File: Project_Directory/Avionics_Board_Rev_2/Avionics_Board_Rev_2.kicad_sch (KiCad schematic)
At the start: 0 parts

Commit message: started working.
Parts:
- added U1: Teensy4.1, symbol VelR:Teensy4.1_1
- added U2: ~, symbol VelR:RFM95W
- added U3: ~, symbol VelR:ADXL-377
- added U4: ~, symbol VelR:NEO-7M

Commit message: temp
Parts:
- removed U4: ~, symbol VelR:NEO-7M
- added U5: ~, symbol VelR:BUCK_CONVERTER
- added U6: ~, symbol VelR:neo-7m
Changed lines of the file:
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@@
 	(paper "A4")
-	(symbol
-		(lib_id "VelR:NEO-7M")
-		(at 237.49 110.49 0)
-		(unit 1)
-		(exclude_from_sim no)
-		(in_bom yes)
-		(on_board yes)
-		(dnp no)
-		(fields_autoplaced yes)
-		(property "Reference" "U4"
-			(at 254 105.3398 0)
-			(effects
-				(font
-					(size 1.27 1.27)
-				)
-			)
-		)
-		(property "Value" "~"
-			(at 254 107.8798 0)
-			(effects
-				(font
-					(size 1.27 1.27)
-				)
-			)
-		)
-		(property "Footprint" ""
-			(at 237.49 110.49 0)
-			(effects
-				(font
-					(size 1.27 1.27)
-				)
-				(hide yes)
-			)
-		)
-		(property "Datasheet" ""
-			(at 237.49 110.49 0)
-			(effects
-				(font
-					(size 1.27 1.27)
-				)
-				(hide yes)
-			)
-		)
-		(property "Description" ""
-			(at 237.49 110.49 0)
-			(effects
-				(font
-					(size 1.27 1.27)
-				)
-				(hide yes)
-			)
-		)
-		(pin "4"
-		)
-		(pin "1"
-		)
-		(pin "3"
-		)
-		(pin "2"
-		)
-		(instances
-			(project ""
-				(path "/d97b3dcb-6a87-4cc6-862f-281d47ed4b8f"
-					(reference "U4")
-					(unit 1)
-				)
-			)
-		)
-	)
 	(symbol
 		(lib_id "VelR:Teensy4.1_1")
@@
 					(unit 1)
 				)
+			)
+		)
+	)
+	(symbol
+		(lib_id "VelR:neo-7m")
+		(at 213.36 107.95 0)
+		(unit 1)
+		(exclude_from_sim no)
+		(in_bom yes)
+		(on_board yes)
+		(dnp no)
+		(fields_autoplaced yes)
+		(property "Reference" "U6"
+			(at 213.36 107.95 0)
+			(effects
+				(font
+					(size 1.27 1.27)
+				)
+				(hide yes)
+			)
+		)
+		(property "Value" "~"
+			(at 219.71 107.9499 0)
+			(effects
+				(font
+					(size 1.27 1.27)
+				)
+				(justify left)
+			)
+		)
+		(property "Footprint" ""
+			(at 213.36 107.95 0)
+			(effects
+				(font
+					(size 1.27 1.27)
+				)
+				(hide yes)
+			)
+		)
+		(property "Datasheet" ""
+			(at 213.36 107.95 0)
+			(effects
+				(font
+					(size 1.27 1.27)
+				)
+				(hide yes)
+			)
+		)
+		(property "Description" ""
+			(at 213.36 107.95 0)
+			(effects
+				(font
+					(size 1.27 1.27)
+				)
+				(hide yes)
+			)
+		)
+		(pin "1"
+		)
+		(pin "3"
+		)
+		(pin "4"
+		)
+		(pin "2"
+		)
+		(instances
+			(project ""
+				(path "/d97b3dcb-6a87-4cc6-862f-281d47ed4b8f"
+					(reference "U6")
+					(unit 1)
+				)
+			)
+		)
+	)
+	(symbol
+		(lib_id "VelR:BUCK_CONVERTER")
+		(at 55.88 96.52 0)
+		(unit 1)
+		(exclude_from_sim no)
+		(in_bom yes)
+		(on_board yes)
+		(dnp no)
+		(fields_autoplaced yes)
+		(property "Reference" "U5"
+			(at 56.515 85.09 0)
+			(effects
+				(font
+					(size 1.27 1.27)
+				)
+			)
+		)
+		(property "Value" "~"
+			(at 56.515 87.63 0)
+			(effects
+				(font
+					(size 1.27 1.27)
+				)
+			)
+		)
+		(property "Footprint" ""
+			(at 55.88 96.52 0)
+			(effects
+				(font
+					(size 1.27 1.27)
+				)
+				(hide yes)
+			)
+		)
+		(property "Datasheet" ""
+			(at 55.88 96.52 0)
+			(effects
+				(font
+					(size 1.27 1.27)
+				)
+				(hide yes)
+			)
+		)
+		(property "Description" ""
+			(at 55.88 96.52 0)
+			(effects
+				(font
+					(size 1.27 1.27)
+				)
+				(hide yes)
+			)
+		)
+		(pin "6"
+		)
+		(pin "4"
+		)
+		(pin "1"
+		)
+		(pin "8"
+		)
+		(pin "5"
+		)
+		(pin "3"
+		)
+		(pin "2"
+		)
+		(pin "7"
+		)
+		(instances
+			(project ""
+				(path "/d97b3dcb-6a87-4cc6-862f-281d47ed4b8f"
+					(reference "U5")
+					(unit 1)
+				)

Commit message: schematic
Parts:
- removed U5: ~, symbol VelR:BUCK_CONVERTER
- added Buck_Converter: ~, symbol VelR3:BUCK_CONVERTER_new
- added J1: Battery, symbol Connector:Conn_01x02_Pin
- added J10: PWM_1, symbol Connector:Conn_01x03_Pin
- added J11: PWM_2, symbol Connector:Conn_01x03_Pin
- added J12: PWM_3, symbol Connector:Conn_01x03_Pin
- added J13: I2C, symbol Connector:Conn_01x04_Pin
- added J14: UART, symbol Connector:Conn_01x04_Pin
- added J2: ARM, symbol Connector:Conn_01x02_Pin
- added J3: PYRO_1, symbol Connector:Conn_01x02_Pin
- added J7: PWM_4, symbol Connector:Conn_01x03_Pin
- added J8: PWM_5, symbol Connector:Conn_01x03_Pin
- added J9: PWM_6, symbol Connector:Conn_01x03_Pin
- added Q1: IRF026, symbol Simulation_SPICE:NMOS
- added Q2: Drive_MOS, symbol Simulation_SPICE:NMOS
- added R1, R2, R3, R4, R5: R, symbol Device:R
- added U4: AMS1117-5.0, Package_TO_SOT_SMD:SOT-223-3_TabPin2, symbol Regulator_Linear:AMS1117-5.0
- added U5: AMS1117-3.3, Package_TO_SOT_SMD:SOT-223-3_TabPin2, symbol Regulator_Linear:AMS1117-3.3
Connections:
- net +3.3V: now reaches U1.51 (3V3)
- net +3.3V: now also U2.4 (3.3V), U3.2 (3.3V), U6.1 (VCC), J13.1 (Pin_1), J14.1 (Pin_1), R3.2
- net GND: now reaches U1.52 (GND)
- net GND: now also U2.7 (GND), U6.4 (GND), J10.3 (Pin_3), J11.3 (Pin_3), J12.3 (Pin_3), J13.4 (Pin_4), J14.4 (Pin_4), J7.3 (Pin_3), J8.3 (Pin_3), J9.3 (Pin_3), Q2.3 (S), R5.2
- new net: Q1.2 (G), Q2.1 (D), R1.2
- new net: Buck_Converter.1 (Vin), Buck_Converter.2 (Vin)
- new net: Buck_Converter.3 (Vin), Buck_Converter.4 (Vin)
- new net: J3.1 (Pin_1), Q1.1 (D), R4.1
- new net +5V: J10.2 (Pin_2), J11.2 (Pin_2), J12.2 (Pin_2), J7.2 (Pin_2), J8.2 (Pin_2), J9.2 (Pin_2)
- new net +BATT: Buck_Converter.5 (Vout), Buck_Converter.6 (Vout), J1.1 (Pin_1), J2.1 (Pin_1), R2.1
- new net +VDC: J2.2 (Pin_2), J3.2 (Pin_2), R1.1, R2.2
- new net GNDPWR: Buck_Converter.7 (Vout), Buck_Converter.8 (Vout), J1.2 (Pin_2), Q1.3 (S)
- new net PYRO_1_Trig: Q2.2 (G), R3.1
- new net PYRO_1_continuity: R4.2, R5.1

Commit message: working
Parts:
- added D1: B120-E3, Diode_SMD:D_SMA, symbol VelR7:B120-E3
- added U7: ~, symbol VelR8:gy-91
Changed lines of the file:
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@@
+	)
+	(symbol
+		(lib_id "VelR7:B120-E3")
+		(at 229.87 99.06 0)
+		(unit 1)
+		(exclude_from_sim no)
+		(in_bom yes)
+		(on_board yes)
+		(dnp no)
+		(fields_autoplaced yes)
+		(property "Reference" "D1"
+			(at 229.5525 92.71 0)
+			(effects
+				(font
+					(size 1.27 1.27)
+				)
+			)
+		)
+		(property "Value" "B120-E3"
+			(at 229.5525 95.25 0)
+			(effects
+				(font
+					(size 1.27 1.27)
+				)
+			)
+		)
+		(property "Footprint" "Diode_SMD:D_SMA"
+			(at 229.87 103.505 0)
+			(effects
+				(font
+					(size 1.27 1.27)
+				)
+				(hide yes)
+			)
+		)
+		(property "Datasheet" "http://www.vishay.com/docs/88946/b120.pdf"
+			(at 229.87 99.06 0)
+			(effects
+				(font
+					(size 1.27 1.27)
+				)
+				(hide yes)
+			)
+		)
+		(property "Description" "20V 1A Schottky Barrier Rectifier Diode, SMA(DO-214AC)"
+			(at 229.87 99.06 0)
+			(effects
+				(font
+					(size 1.27 1.27)
+				)
+				(hide yes)
+			)
+		)
+		(pin "1"
+		)
+		(pin "2"
+		)
+		(instances
+			(project ""
+				(path "/d97b3dcb-6a87-4cc6-862f-281d47ed4b8f"
+					(reference "D1")
+					(unit 1)
+				)
+			)
+		)
 	)
 	(symbol
@@
 					(unit 1)
 				)
+			)
+		)
+	)
+	(symbol
+		(lib_id "VelR8:gy-91")
+		(at 193.04 82.55 0)
+		(unit 1)
+		(exclude_from_sim no)
+		(in_bom yes)
+		(on_board yes)
+		(dnp no)
+		(fields_autoplaced yes)
+		(property "Reference" "U7"
+			(at 201.93 81.2799 0)
+			(effects
+				(font
+					(size 1.27 1.27)
+				)
+				(justify left)
+			)
+		)
+		(property "Value" "~"
+			(at 201.93 83.8199 0)
+			(effects
+				(font
+					(size 1.27 1.27)
+				)
+				(justify left)
+			)
+		)
+		(property "Footprint" ""
+			(at 193.04 82.55 0)
+			(effects
+				(font
+					(size 1.27 1.27)
+				)
+				(hide yes)
+			)
+		)
+		(property "Datasheet" ""
+			(at 193.04 82.55 0)
+			(effects
+				(font
+					(size 1.27 1.27)
+				)
+				(hide yes)
+			)
+		)
+		(property "Description" ""
+			(at 193.04 82.55 0)
+			(effects
+				(font
+					(size 1.27 1.27)
+				)
+				(hide yes)
+			)
+		)
+		(pin "6"
+		)
+		(pin "4"
+		)
+		(pin "7"
+		)
+		(pin "1"
+		)
+		(pin "8"
+		)
+		(pin "5"
+		)
+		(pin "2"
+		)
+		(pin "3"
+		)
+		(instances
+			(project ""
+				(path "/d97b3dcb-6a87-4cc6-862f-281d47ed4b8f"
+					(reference "U7")
+					(unit 1)
+				)

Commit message: in progess
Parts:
- removed Q1: IRF026, symbol Simulation_SPICE:NMOS
- removed U4: AMS1117-5.0, Package_TO_SOT_SMD:SOT-223-3_TabPin2, symbol Regulator_Linear:AMS1117-5.0
- added C1, C7: IRFR024NPBF, symbol VelR6:IRFR024NPBF MOSFET
- added C2, C3, C4, C5, C6: ~, C2012X7R2A104K125AA:CAPC2012X145N, symbol VelR6:0805-Decoupling capacitor
- added D2: D_Zener, symbol Device:D_Zener
- added R6: R, symbol Device:R
- added U10: ~, symbol VelR5:GSM_Module
- added U4: AMS1117-3.3, Package_TO_SOT_SMD:SOT-223-3_TabPin2, symbol Regulator_Linear:AMS1117-3.3
- added U8: AMS1117-5.0, Package_TO_SOT_SMD:SOT-223-3_TabPin2, symbol Regulator_Linear:AMS1117-5.0
- added U9: ADS1115 ADC, Package_SO:TSSOP-10_3x3mm_P0.5mm, symbol Analog_ADC:ADS1115IDGS
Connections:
- net +3.3V: now also U7.2 (3v3), C6.1, U4.2 (VO), U9.8 (VDD); no longer R3.2
- net +5V: now also C5.2, U8.2 (VO)
- net +BATT: now also U5.3 (VI), C2.1, C4.1, R6.1, U8.3 (VI)
- net +VDC: now also D1.1 (K)
- net GND: now also U3.1 (GND), U5.1 (GND), U7.3 (gnd), C2.2, C3.1, C4.2, C5.1, C6.2, U10.6 (GND), U8.1 (GND), U9.3 (GND)
- net GNDPWR: now also C1.3, C7.3, D2.2 (A); no longer J1.2 (Pin_2)
- net at Q2.1 (D), R1.2: now also C1.1
- net PWM_2: now reaches J11.1 (Pin_1)
- net PWM_4: now reaches J7.1 (Pin_1)
- net PWM_6: now reaches J9.1 (Pin_1)
- net SPI0_MOSI: now reaches U1.13 (11_MOSI_CTX1)
- net SPI0_MOSI: now also U7.5 (sda)
- net SPI0_MISO: now reaches U1.14 (12_MISO_MQSL)
- net SPI0_MISO: now also U7.6 (sdo/sao)
- net SPI1_MOSI: now reaches U1.18 (26_A12_MOSI1)
- net SPI1_SCK: now reaches U1.19 (27_A13_SCK1)
- net CS_IMU: now reaches U1.22 (30_CRX3)
- net CS_IMU: now also U7.7 (ncs)
- net CS_BMP: now reaches U1.23 (31_CTX3)
- net CS_BMP: now also U7.8 (csb)
- net GSM_RST: now reaches U1.24 (32_OUT1B)
- net GSM_RST: now also U10.3 (RST)
- net GSM_TX: now reaches U1.26 (34_RX8)
- net GSM_TX: now also U10.5 (TXD)
- net GSM_RX: now reaches U1.27 (35_TX8)
- net GSM_RX: now also U10.4 (RXD)
- net SPI1_MISO: now reaches U1.3 (1_TX1_CTX2_MISO1)
- net SPI0_SCK: now reaches U1.35 (13_SCK_LED)
- net SPI0_SCK: now also U7.4 (scl)
- net I2C1_SCL: now reaches U1.38 (16_A2_RX4_SCL1)
- net I2C1_SCL: now also U9.10 (SCL)
- net I2C1_SDA: now reaches U1.39 (17_A3_TX4_SDA1)
- net I2C1_SDA: now also U9.9 (SDA)
- net GPS_RX: now reaches U1.42 (20_A6_TX5_LRCLK1)
- net GPS_RX: now also U6.2 (RX)
- net GPS_TX: now reaches U1.43 (21_A7_RX5_BCLK1)
- net GPS_TX: now also U6.3 (TX)
- net at Buck_Converter.1 (Vin), Buck_Converter.2 (Vin): now also U4.1 (GND)
- net BUCK_Out: now reaches Buck_Converter.3 (Vin), Buck_Converter.4 (Vin)
- net BUCK_Out: now also U10.2 (VCC), U4.3 (VI)
- net at D1.2 (A): now also J3.1 (Pin_1), R4.1, C1.4
- net Spare_UART_TX: now reaches J14.2 (Pin_2)
- net Spare_UART_RX: now reaches J14.3 (Pin_3)
- net at U3.3 (X): now also U9.7 (AIN3)
- net at U3.4 (Y): now also U9.6 (AIN2)
- net at U3.5 (Z): now also U9.5 (AIN1)
- net ADXL_ST: now reaches U3.6 (ST)
- net +3.3VP: now reaches U5.2 (VO)
- net +3.3VP: now also R3.2, C3.2
- net PWM_3: now reaches J12.1 (Pin_1)
- net PWM_5: now reaches J8.1 (Pin_1)
- net Spare_I2C_SCL: now reaches J13.2 (Pin_2)
- net Spare_I2C_SDA: now reaches J13.3 (Pin_3)
- net PWM_1: now reaches J10.1 (Pin_1)
- new net: C7.1, D2.1 (K), R6.2
- new net: C7.4, J1.2 (Pin_2)
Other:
- moved on the sheet: Buck_Converter, D1, J1, J10, J11, J12, J14, J3, J7, J8, J9, Q2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

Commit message: progress on schematic and pcb
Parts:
- added C10, C8, C9: IRFR024NPBF, VelR:IRFR024NTRPBF-HXY Mosfet, symbol VelR6:IRFR024NPBF MOSFET
- added D3, D4, D5: B120-E3, Diode_SMD:D_SMA, symbol VelR7:B120-E3
- added J4, J5, J6: PYRO_1, TerminalBlock_Phoenix:TerminalBlock_Phoenix_MKDS-1,5-2_1x02_P5.00mm_Horizontal, symbol Connector:Conn_01x02_Pin
- added Q1, Q3, Q4: Drive_MOS, symbol Simulation_SPICE:NMOS
- added R10, R11, R12, R13, R14, R15, R16, R17, R18, R7, R8, R9: R, symbol Device:R
- Buck_Converter1: renamed from Buck_Converter; value ~ -> buck converter; footprint (none) -> VelR:buck converter
- C1, C7: footprint (none) -> VelR:IRFR024NTRPBF-HXY Mosfet
- D2: footprint (none) -> VelR:diode_
- J1, J2: footprint (none) -> TerminalBlock_Phoenix:TerminalBlock_Phoenix_MKDS-1,5-2-5.08_1x02_P5.08mm_Horizontal
- J10, J11, J12, J7, J8, J9: footprint (none) -> Connector_PinHeader_2.54mm:PinHeader_1x03_P2.54mm_Vertical
- J13, J14: footprint (none) -> Connector_JST:JST_EH_B4B-EH-A_1x04_P2.50mm_Vertical
- J3: footprint (none) -> TerminalBlock_Phoenix:TerminalBlock_Phoenix_MKDS-1,5-2_1x02_P5.00mm_Horizontal
- U1: footprint (none) -> VelR:Teensy_4.1
- U10: value ~ -> GSM; footprint (none) -> VelR:SIM800L
- U2: value ~ -> LoRa; footprint (none) -> VelR:RFM95W
- U3: value ~ -> ADXL
- U6: value ~ -> GPS; footprint (none) -> VelR:JST-SH 1mm 4 Pin Male E Type Vertical Single Row WTB Connector
- U7: value ~ -> GY-91; footprint (none) -> VelR:gy91
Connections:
- net +3.3VP: now also R11.2, R15.2, R7.2
- net +VDC: now also D3.1 (K), D4.1 (K), D5.1 (K), J4.2 (Pin_2), J5.2 (Pin_2), J6.2 (Pin_2), R12.1, R16.1, R8.1
- net GND: now also Q1.3 (S), Q3.3 (S), Q4.3 (S), R10.2, R14.2, R18.2
- net GNDPWR: now also C10.3, C8.3, C9.3
- new net: C8.1, Q1.1 (D), R8.2
- new net: C8.4, D3.2 (A), J4.1 (Pin_1), R9.1
- new net: C9.4, D4.2 (A), J5.1 (Pin_1), R13.1
- new net: C10.1, Q4.1 (D), R16.2
- new net: C10.4, D5.2 (A), J6.1 (Pin_1), R17.1
- new net: C9.1, Q3.1 (D), R12.2
- new net PYRO_2_Trig: Q3.2 (G), R11.1
- new net PYRO_2_continuity: R13.2, R14.1
- new net PYRO_3_Trig: Q1.2 (G), R7.1
- new net PYRO_3_continuity: R10.1, R9.2
- new net PYRO_4_Trig: Q4.2 (G), R15.1
- new net PYRO_4_continuity: R17.2, R18.1
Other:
- moved on the sheet: Buck_Converter1, C1, C2, C3, C4, C5, C6, C7, D1, D2, J1, J3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

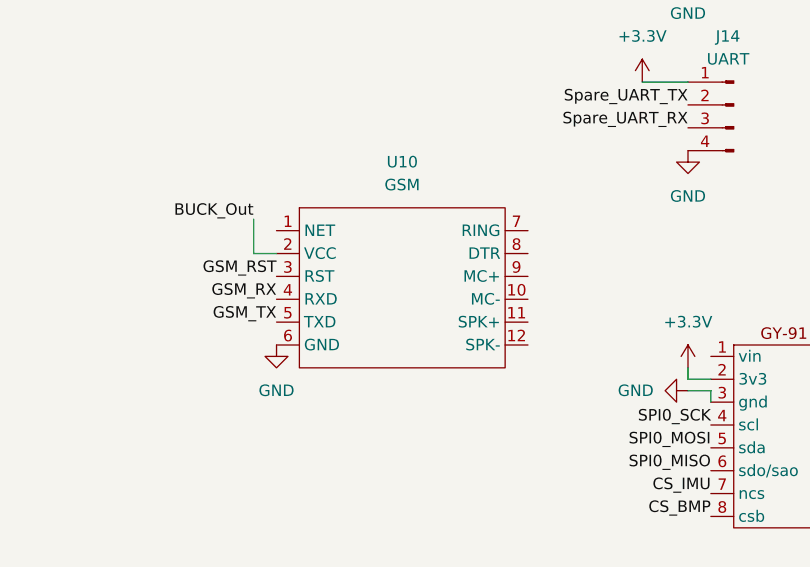
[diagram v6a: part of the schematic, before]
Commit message: modified gsm to be a jst connector
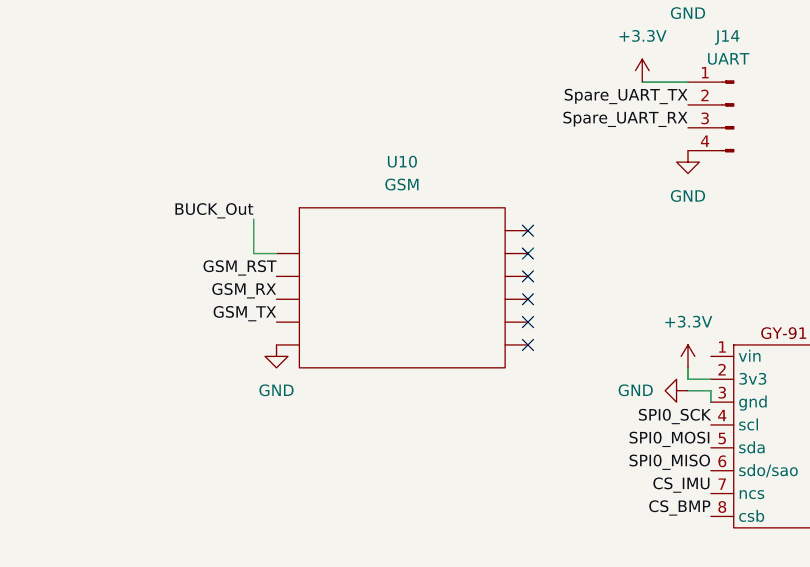
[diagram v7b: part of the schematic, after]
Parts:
- U10: footprint VelR:SIM800L -> Connector_JST:JST_EH_B5B-EH-A_1x05_P2.50mm_Vertical
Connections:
- no-connect marks 0 -> 6
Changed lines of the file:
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@@
 		(color 0 0 0 0)
 	)
+	(no_connect
+		(at 248.92 72.39)
+	)
+	(no_connect
+		(at 248.92 69.85)
+	)
+	(no_connect
+		(at 248.92 62.23)
+	)
+	(no_connect
+		(at 248.92 59.69)
+	)
+	(no_connect
+		(at 248.92 67.31)
+	)
+	(no_connect
+		(at 248.92 64.77)
+	)
 	(wire
 		(pts
@@
 			)
 		)
-		(property "Footprint" "VelR:SIM800L"
+		(property "Footprint" "Connector_JST:JST_EH_B5B-EH-A_1x05_P2.50mm_Vertical"
 			(at 234.95 66.04 0)
 			(effects
@@
 		(pin "6"
 		)
-		(pin "1"
-		)
 		(pin "7"

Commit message: changes to schematic
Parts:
- removed U2: LoRa, VelR:RFM95W, symbol VelR:RFM95W
- added C11, C12: ~, Capacitor_SMD:C_0603_1608Metric_Pad1.08x0.95mm_HandSolder, symbol VelR6:0805-Decoupling capacitor
- added JP1: SolderJumper_3_Open, Jumper:SolderJumper-3_P2.0mm_Open_TrianglePad1.0x1.5mm, symbol Jumper:SolderJumper_3_Open
- added U2: LoRa - RFM95-W/PW, VelR:RFM95W,PW, symbol VelR9:RFM95_W/PW
- C2, C3, C4, C5, C6: footprint C2012X7R2A104K125AA:CAPC2012X145N -> Capacitor_SMD:C_0603_1608Metric_Pad1.08x0.95mm_HandSolder
- R1, R10, R11, R12, R13, R14, R15, R16, R17, R18, R2, R3, R4, R5, R6, R7, R8, R9: footprint (none) -> Resistor_SMD:R_1206_3216Metric_Pad1.30x1.75mm_HandSolder
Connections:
- net +3.3V: now also C12.2, JP1.1 (A), U2.17 (3.3)
- net +5V: now also JP1.3 (B)
- net BUCK_Out: now also C11.2
- net GND: now also U2.1 (GND), U2.10 (GND), U2.8 (GND)
- net PWM_1: now also U1.17 (25_A11_RX6_SDA2)
- net PWM_2: now also U1.20 (28_RX7)
- net PWM_3: now also U1.21 (29_TX7)
- net PWM_4: now also U1.25 (33_MCLK2)
- net PWM_5: now also U1.28 (36_CS)
- net PWM_6: now also U1.29 (37_CS)
- net SPI1_MISO: now also U2.2 (MISO)
- net SPI1_MOSI: now also U2.3 (MOSI)
- net SPI1_SCK: now also U2.4 (SCK)
- net LoRa_INT: now reaches U1.4 (2_OUT2)
- net LoRa_INT: now also U2.14 (DIO0)
- net LoRa_DIO1: now reaches U1.5 (3_LRCLK2)
- net LoRa_DIO1: now also U2.15 (DIO1)
- net LoRa_CS: now reaches U1.6 (4_BCLK2)
- net LoRa_CS: now also U2.5 (NSS)
- net LoRa_RST: now reaches U1.7 (5_IN2)
- net LoRa_RST: now also U2.6 (RESET)
- net at Buck_Converter1.1 (Vin), Buck_Converter1.2 (Vin), U4.1 (GND): now also C11.1, C12.1
- new net: JP1.2 (C), U2.13 (3.3/5)
